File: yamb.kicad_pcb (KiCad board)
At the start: 2 copper layers, 68.7 x 110.2 mm, 18 parts, among them J1 Barrel_Jack, J2 I2C, J4 HEADER_2.54, J5 Remote_Reset, J6 Power_Switch, P1 USB_C_Plug_USB2.0, SW1 RESET, U1 TPS3808DBV, U2 MCSBC, U3 SVR, U4 RAK4630, U5 BME280

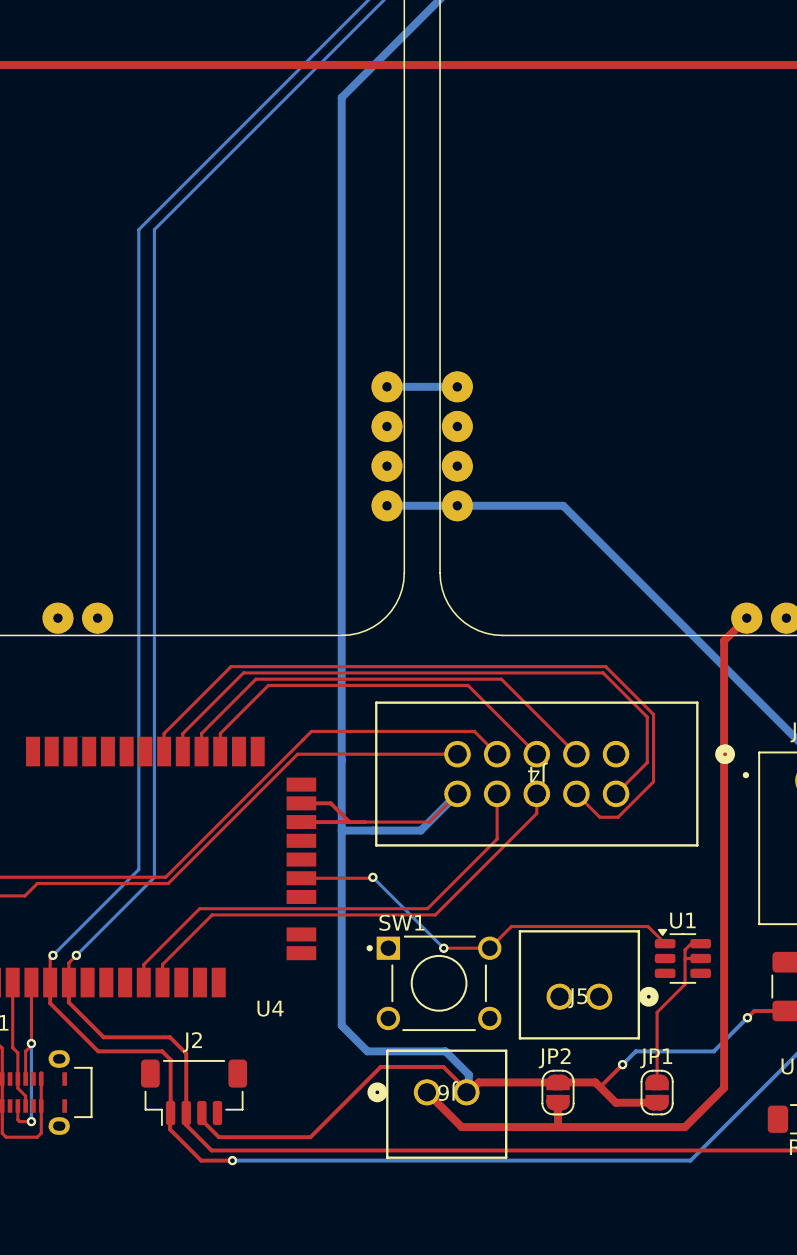
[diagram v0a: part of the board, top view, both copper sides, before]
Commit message: fixed remaining DRC errors
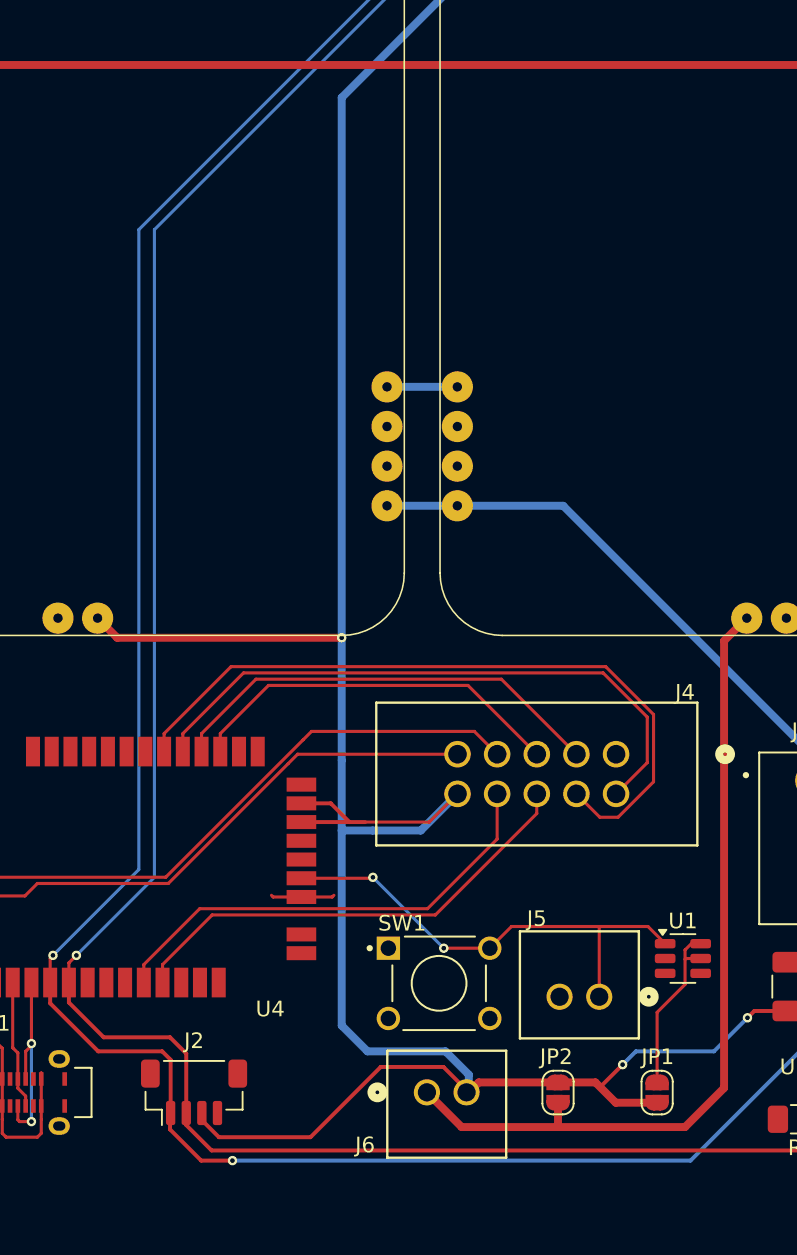
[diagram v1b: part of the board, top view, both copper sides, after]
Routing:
- net 3V3: track 170.7 -> 186.9 mm, vias 2 -> 3
- net RESET: track 26.4 -> 30.9 mm
- net GND: track 3.62 -> 7.71 mm
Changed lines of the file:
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@@
 		(tags "705430036 ")
 		(property "Reference" "J6"
-			(at -1.27 0 180)
+			(at 3.96 -3.375 0)
 			(unlocked yes)
 			(layer "F.SilkS")
@@
 		(tags "705430036 ")
 		(property "Reference" "J5"
-			(at -1.27 0 0)
+			(at -4 -5 0)
 			(unlocked yes)
 			(layer "F.SilkS")
@@
 		(tags "702461004 ")
 		(property "Reference" "J4"
-			(at 5.08 -1.27 180)
+			(at -4.42 3.96 0)
 			(unlocked yes)
 			(layer "F.SilkS")
@@
 	)
 	(segment
+		(start 133.419997 98.108002)
+		(end 131.608002 98.108002)
+		(width 0.2)
+		(layer "F.Cu")
+		(net 3)
+	)
+	(segment
 		(start 110.42 99.241)
 		(end 112.109 99.241)
@@
 	)
 	(segment
+		(start 131.608002 98.108002)
+		(end 131.5 98)
+		(width 0.2)
+		(layer "F.Cu")
+		(net 3)
+	)
+	(segment
+		(start 133.419997 98.108002)
+		(end 135.391998 98.108002)
+		(width 0.2)
+		(layer "F.Cu")
+		(net 3)
+	)
+	(segment
+		(start 135.5 98)
+		(end 135.391998 98.108002)
+		(width 0.2)
+		(layer "F.Cu")
+		(net 3)
+	)
+	(segment
 		(start 138.058002 96.908002)
 		(end 138 96.85)
@@
 	)
 	(segment
+		(start 155.625 100)
+		(end 152.5 100)
+		(width 0.2)
+		(layer "F.Cu")
+		(net 5)
+	)
+	(segment
 		(start 156.725 101.1)
 		(end 155.625 100)
@@
 	)
 	(segment
-		(start 155.625 100)
+		(start 152.5 100)
 		(end 146.88 100)
 		(width 0.2)
@@
 		(net 5)
 	)
+	(segment
+		(start 152.5 104.5)
+		(end 152.5 100)
+		(width 0.2)
+		(layer "F.Cu")
+		(net 5)
+	)
 	(via
 		(at 142.54 101.39)
@@
 	)
 	(segment
+		(start 121.6175 81.5)
+		(end 136 81.5)
+		(width 0.508)
+		(layer "F.Cu")
+		(net 52)
+	)
+	(segment
 		(start 152.26 109.99)
 		(end 149.86 109.99)
@@
 	)
 	(segment
+		(start 120.359501 80.242001)
+		(end 121.6175 81.5)
+		(width 0.508)
+		(layer "F.Cu")
+		(net 52)
+	)
+	(segment
 		(start 141.611998 93.308002)
 		(end 137.5 93.308002)
@@
 	)
 	(via
+		(at 136 81.5)
+		(size 0.6)
+		(drill 0.3)
+		(layers "F.Cu" "B.Cu")
+		(net 52)
+	)
+	(via
 		(at 154 108.85)
 		(size 0.6)
@@
 	)
 	(segment
-		(start 136 89.35)
+		(start 136 81.5)
 		(end 136 46.888)
 		(width 0.508)
@@
 		(width 0.508)
 		(layer "B.Cu")
+		(net 52)
+	)
+	(segment
+		(start 136 89.35)
+		(end 136 81.5)
+		(width 0.508)
+		(layer "B.Cu")
